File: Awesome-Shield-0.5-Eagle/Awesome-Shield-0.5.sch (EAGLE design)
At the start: 14 parts, among them J1 ARDUINO_R3_SHIELDUNO_R3_SHIEL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, SW1 SPST_TACT-EVQQ2

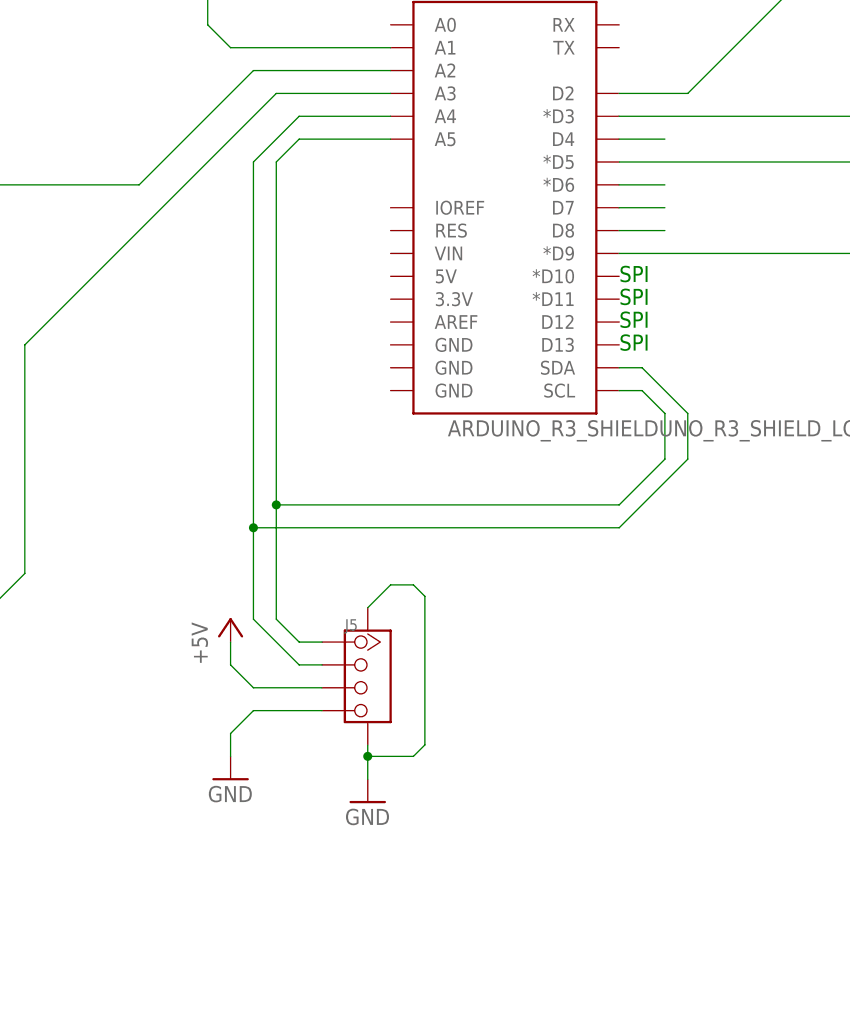
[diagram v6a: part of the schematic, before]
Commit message: placed grove ports in layout, added A4 A5 SCL SDA jumpers in schematic
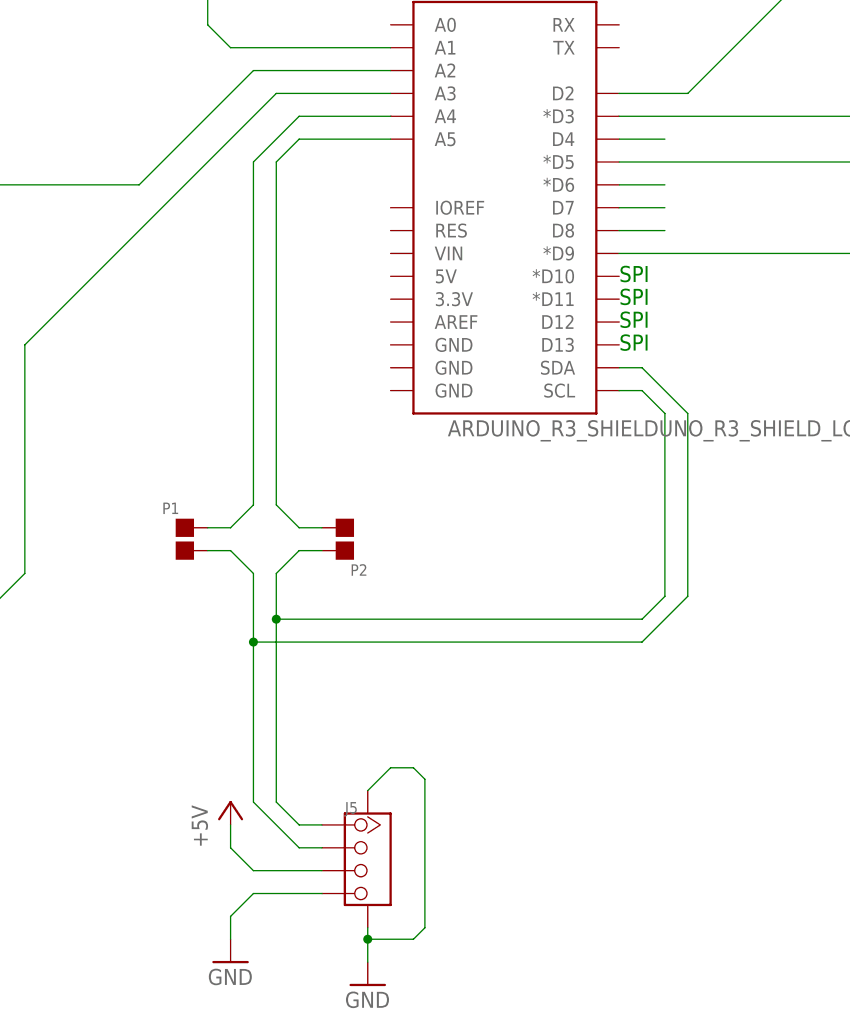
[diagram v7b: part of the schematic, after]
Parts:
- added P1, P2: DNP, Discrete:PAD-JUMPER-2P
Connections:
- new net SCL: J1.SCL, J5.1, P2.2
- new net SDA: J1.SDA, J5.2, P1.1
- net A4: now also P1.2; no longer J1.SDA, J5.2
- net A5: now also P2.1; no longer J1.SCL, J5.1
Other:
- moved on the sheet: J5
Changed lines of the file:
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@@
 </variantdefs>
 <classes>
-<class number="0" name="default" width="0" drill="0">
+<class number="0" name="default" width="0.2032" drill="0.3048">
+<clearance class="0" value="0.1524"/>
 </class>
 </classes>
@@
 <part name="J3" library="Connector " deviceset="TWIG-4P-2.0-SMD-FEMALE-REINFORCE" device="'DD'"/>
 <part name="GND11" library="supply1" deviceset="GND" device=""/>
+<part name="P1" library="Discrete" deviceset="PAD-JUMPER-2P" device="" value="DNP"/>
+<part name="P2" library="Discrete" deviceset="PAD-JUMPER-2P" device="" value="DNP"/>
 </parts>
 <sheets>
@@
 <instance part="+3V3" gate="G$1" x="187.96" y="226.06"/>
 <instance part="GND5" gate="1" x="269.24" y="190.5"/>
-<instance part="GND6" gate="1" x="165.1" y="66.04"/>
-<instance part="P+1" gate="1" x="165.1" y="83.82"/>
+<instance part="GND6" gate="1" x="165.1" y="45.72"/>
+<instance part="P+1" gate="1" x="165.1" y="63.5"/>
 <instance part="GND7" gate="1" x="269.24" y="73.66"/>
 <instance part="P+2" gate="1" x="269.24" y="91.44"/>
 <instance part="P+3" gate="1" x="309.88" y="91.44"/>
 <instance part="GND8" gate="1" x="309.88" y="73.66"/>
-<instance part="J5" gate="G$1" x="180.34" y="77.47"/>
-<instance part="GND9" gate="1" x="180.34" y="63.5"/>
+<instance part="J5" gate="G$1" x="180.34" y="57.15"/>
+<instance part="GND9" gate="1" x="180.34" y="43.18"/>
 <instance part="J2" gate="G$1" x="287.02" y="85.09"/>
 <instance part="GND10" gate="1" x="287.02" y="71.12"/>
 <instance part="J3" gate="G$1" x="327.66" y="85.09"/>
 <instance part="GND11" gate="1" x="327.66" y="71.12"/>
+<instance part="P1" gate="G$1" x="160.02" y="92.71"/>
+<instance part="P2" gate="G$1" x="177.8" y="92.71" rot="R180"/>
 </instances>
 <busses>
@@
 </segment>
 <segment>
-<wire x1="167.64" y1="73.66" x2="165.1" y2="71.12" width="0.1524" layer="91"/>
-<wire x1="165.1" y1="71.12" x2="165.1" y2="68.58" width="0.1524" layer="91"/>
+<wire x1="167.64" y1="53.34" x2="165.1" y2="50.8" width="0.1524" layer="91"/>
+<wire x1="165.1" y1="50.8" x2="165.1" y2="48.26" width="0.1524" layer="91"/>
 <pinref part="GND6" gate="1" pin="GND"/>
 <pinref part="J5" gate="G$1" pin="4"/>
-<wire x1="167.64" y1="73.66" x2="175.26" y2="73.66" width="0.1524" layer="91"/>
+<wire x1="167.64" y1="53.34" x2="175.26" y2="53.34" width="0.1524" layer="91"/>
 </segment>
 <segment>
@@
 <segment>
 <pinref part="J5" gate="G$1" pin="SS1"/>
-<wire x1="180.34" y1="85.09" x2="182.88" y2="87.63" width="0.1524" layer="91"/>
-<wire x1="182.88" y1="87.63" x2="185.42" y2="87.63" width="0.1524" layer="91"/>
-<wire x1="185.42" y1="87.63" x2="186.69" y2="86.36" width="0.1524" layer="91"/>
-<wire x1="186.69" y1="86.36" x2="186.69" y2="69.85" width="0.1524" layer="91"/>
-<wire x1="186.69" y1="69.85" x2="185.42" y2="68.58" width="0.1524" layer="91"/>
-<wire x1="185.42" y1="68.58" x2="180.34" y2="68.58" width="0.1524" layer="91"/>
+<wire x1="180.34" y1="64.77" x2="182.88" y2="67.31" width="0.1524" layer="91"/>
+<wire x1="182.88" y1="67.31" x2="185.42" y2="67.31" width="0.1524" layer="91"/>
+<wire x1="185.42" y1="67.31" x2="186.69" y2="66.04" width="0.1524" layer="91"/>
+<wire x1="186.69" y1="66.04" x2="186.69" y2="49.53" width="0.1524" layer="91"/>
+<wire x1="186.69" y1="49.53" x2="185.42" y2="48.26" width="0.1524" layer="91"/>
+<wire x1="185.42" y1="48.26" x2="180.34" y2="48.26" width="0.1524" layer="91"/>
 <pinref part="J5" gate="G$1" pin="SS2"/>
-<wire x1="180.34" y1="68.58" x2="180.34" y2="69.85" width="0.1524" layer="91"/>
+<wire x1="180.34" y1="48.26" x2="180.34" y2="49.53" width="0.1524" layer="91"/>
 <pinref part="GND9" gate="1" pin="GND"/>
-<wire x1="180.34" y1="68.58" x2="180.34" y2="66.04" width="0.1524" layer="91"/>
-<junction x="180.34" y="68.58"/>
+<wire x1="180.34" y1="48.26" x2="180.34" y2="45.72" width="0.1524" layer="91"/>
+<junction x="180.34" y="48.26"/>
 </segment>
 <segment>
@@
 <net name="A4" class="0">
 <segment>
-<wire x1="172.72" y1="78.74" x2="167.64" y2="83.82" width="0.1524" layer="91"/>
-<wire x1="167.64" y1="83.82" x2="167.64" y2="93.98" width="0.1524" layer="91"/>
-<wire x1="167.64" y1="93.98" x2="167.64" y2="134.62" width="0.1524" layer="91"/>
 <wire x1="167.64" y1="134.62" x2="172.72" y2="139.7" width="0.1524" layer="91"/>
 <pinref part="J1" gate="G$1" pin="A4"/>
 <wire x1="172.72" y1="139.7" x2="182.88" y2="139.7" width="0.1524" layer="91"/>
-<pinref part="J1" gate="G$1" pin="SDA"/>
-<wire x1="208.28" y1="111.76" x2="210.82" y2="111.76" width="0.1524" layer="91"/>
-<wire x1="210.82" y1="111.76" x2="215.9" y2="106.68" width="0.1524" layer="91"/>
-<wire x1="215.9" y1="106.68" x2="215.9" y2="101.6" width="0.1524" layer="91"/>
-<wire x1="215.9" y1="101.6" x2="208.28" y2="93.98" width="0.1524" layer="91"/>
-<wire x1="208.28" y1="93.98" x2="167.64" y2="93.98" width="0.1524" layer="91"/>
-<junction x="167.64" y="93.98"/>
-<pinref part="J5" gate="G$1" pin="2"/>
-<wire x1="172.72" y1="78.74" x2="175.26" y2="78.74" width="0.1524" layer="91"/>
+<pinref part="P1" gate="G$1" pin="2"/>
+<wire x1="165.1" y1="93.98" x2="162.56" y2="93.98" width="0.1524" layer="91"/>
+<wire x1="167.64" y1="96.52" x2="165.1" y2="93.98" width="0.1524" layer="91"/>
+<wire x1="167.64" y1="134.62" x2="167.64" y2="96.52" width="0.1524" layer="91"/>
 </segment>
 </net>
@@
 <wire x1="182.88" y1="137.16" x2="172.72" y2="137.16" width="0.1524" layer="91"/>
 <wire x1="172.72" y1="137.16" x2="170.18" y2="134.62" width="0.1524" layer="91"/>
-<wire x1="170.18" y1="134.62" x2="170.18" y2="96.52" width="0.1524" layer="91"/>
-<wire x1="170.18" y1="96.52" x2="170.18" y2="83.82" width="0.1524" layer="91"/>
-<wire x1="170.18" y1="83.82" x2="172.72" y2="81.28" width="0.1524" layer="91"/>
-<wire x1="170.18" y1="96.52" x2="208.28" y2="96.52" width="0.1524" layer="91"/>
-<junction x="170.18" y="96.52"/>
-<wire x1="208.28" y1="96.52" x2="213.36" y2="101.6" width="0.1524" layer="91"/>
-<wire x1="213.36" y1="101.6" x2="213.36" y2="106.68" width="0.1524" layer="91"/>
-<wire x1="213.36" y1="106.68" x2="210.82" y2="109.22" width="0.1524" layer="91"/>
-<pinref part="J1" gate="G$1" pin="SCL"/>
-<wire x1="210.82" y1="109.22" x2="208.28" y2="109.22" width="0.1524" layer="91"/>
-<pinref part="J5" gate="G$1" pin="1"/>
-<wire x1="172.72" y1="81.28" x2="175.26" y2="81.28" width="0.1524" layer="91"/>
+<pinref part="P2" gate="G$1" pin="1"/>
+<wire x1="170.18" y1="96.52" x2="172.72" y2="93.98" width="0.1524" layer="91"/>
+<wire x1="172.72" y1="93.98" x2="175.26" y2="93.98" width="0.1524" layer="91"/>
+<wire x1="170.18" y1="96.52" x2="170.18" y2="134.62" width="0.1524" layer="91"/>
 </segment>
 </net>
@@
 <net name="+5V" class="0">
 <segment>
-<wire x1="167.64" y1="76.2" x2="165.1" y2="78.74" width="0.1524" layer="91"/>
-<wire x1="165.1" y1="78.74" x2="165.1" y2="81.28" width="0.1524" layer="91"/>
+<wire x1="167.64" y1="55.88" x2="165.1" y2="58.42" width="0.1524" layer="91"/>
+<wire x1="165.1" y1="58.42" x2="165.1" y2="60.96" width="0.1524" layer="91"/>
 <pinref part="P+1" gate="1" pin="+5V"/>
 <pinref part="J5" gate="G$1" pin="3"/>
-<wire x1="175.26" y1="76.2" x2="167.64" y2="76.2" width="0.1524" layer="91"/>
+<wire x1="175.26" y1="55.88" x2="167.64" y2="55.88" width="0.1524" layer="91"/>
 </segment>
 <segment>
@@
 </segment>
 </net>
+<net name="SDA" class="0">
+<segment>
+<pinref part="J1" gate="G$1" pin="SDA"/>
+<wire x1="208.28" y1="111.76" x2="210.82" y2="111.76" width="0.1524" layer="91"/>
+<wire x1="210.82" y1="111.76" x2="215.9" y2="106.68" width="0.1524" layer="91"/>
+<wire x1="215.9" y1="106.68" x2="215.9" y2="86.36" width="0.1524" layer="91"/>
+<wire x1="215.9" y1="86.36" x2="210.82" y2="81.28" width="0.1524" layer="91"/>
+<wire x1="210.82" y1="81.28" x2="167.64" y2="81.28" width="0.1524" layer="91"/>
+<pinref part="P1" gate="G$1" pin="1"/>
+<wire x1="162.56" y1="91.44" x2="165.1" y2="91.44" width="0.1524" layer="91"/>
+<wire x1="165.1" y1="91.44" x2="167.64" y2="88.9" width="0.1524" layer="91"/>
+<pinref part="J5" gate="G$1" pin="2"/>
+<wire x1="172.72" y1="58.42" x2="167.64" y2="63.5" width="0.1524" layer="91"/>
+<wire x1="172.72" y1="58.42" x2="175.26" y2="58.42" width="0.1524" layer="91"/>
+<wire x1="167.64" y1="88.9" x2="167.64" y2="81.28" width="0.1524" layer="91"/>
+<wire x1="167.64" y1="81.28" x2="167.64" y2="63.5" width="0.1524" layer="91"/>
+<junction x="167.64" y="81.28"/>
+</segment>
+</net>
+<net name="SCL" class="0">
+<segment>
+<pinref part="J1" gate="G$1" pin="SCL"/>
+<wire x1="210.82" y1="109.22" x2="208.28" y2="109.22" width="0.1524" layer="91"/>
+<wire x1="213.36" y1="106.68" x2="210.82" y2="109.22" width="0.1524" layer="91"/>
+<wire x1="213.36" y1="106.68" x2="213.36" y2="86.36" width="0.1524" layer="91"/>
+<wire x1="213.36" y1="86.36" x2="210.82" y2="83.82" width="0.1524" layer="91"/>
+<wire x1="210.82" y1="83.82" x2="170.18" y2="83.82" width="0.1524" layer="91"/>
+<pinref part="J5" gate="G$1" pin="1"/>
+<wire x1="170.18" y1="63.5" x2="172.72" y2="60.96" width="0.1524" layer="91"/>
+<wire x1="172.72" y1="60.96" x2="175.26" y2="60.96" width="0.1524" layer="91"/>
+<pinref part="P2" gate="G$1" pin="2"/>
+<wire x1="175.26" y1="91.44" x2="172.72" y2="91.44" width="0.1524" layer="91"/>
+<wire x1="172.72" y1="91.44" x2="170.18" y2="88.9" width="0.1524" layer="91"/>
+<wire x1="170.18" y1="63.5" x2="170.18" y2="83.82" width="0.1524" layer="91"/>
+<wire x1="170.18" y1="83.82" x2="170.18" y2="88.9" width="0.1524" layer="91"/>
+<junction x="170.18" y="83.82"/>
+</segment>
+</net>

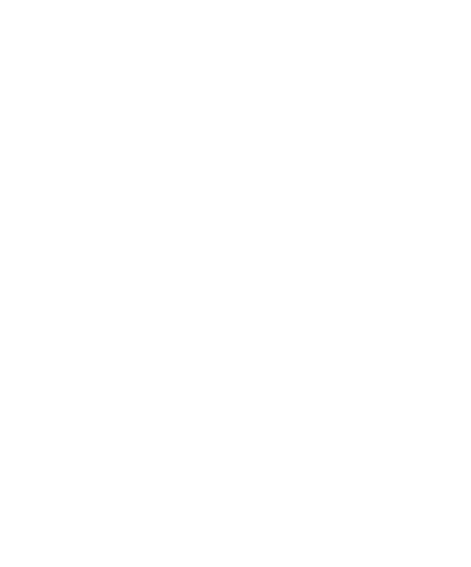
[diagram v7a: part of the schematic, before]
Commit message: added switch -NC, moved RGB LED group
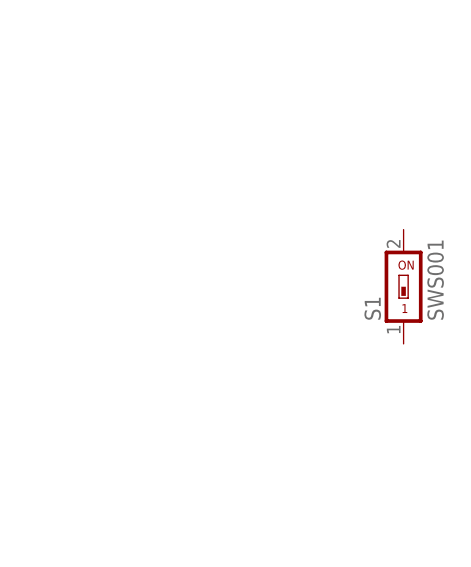
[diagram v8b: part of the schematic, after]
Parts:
- added S1: SWS001, smd-special:SWS001
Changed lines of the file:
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@@
 <part name="P1" library="Discrete" deviceset="PAD-JUMPER-2P" device="" value="DNP"/>
 <part name="P2" library="Discrete" deviceset="PAD-JUMPER-2P" device="" value="DNP"/>
+<part name="S1" library="smd-special" deviceset="SWS001" device=""/>
 </parts>
 <sheets>
@@
 <instance part="P1" gate="G$1" x="160.02" y="92.71"/>
 <instance part="P2" gate="G$1" x="177.8" y="92.71" rot="R180"/>
+<instance part="S1" gate="G$1" x="335.28" y="190.5"/>
 </instances>
 <busses>
